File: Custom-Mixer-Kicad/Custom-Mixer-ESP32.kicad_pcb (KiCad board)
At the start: 2 copper layers, 176.3 x 110.6 mm, 25 parts, among them J1 OLED1, J2 OLED2, J3 OLED3, J4 OLED4, J5 OLED5, SW1 RotaryEncoder_Switch, SW2 RotaryEncoder_Switch, U1 ESP32-DevKitC, U2 2717

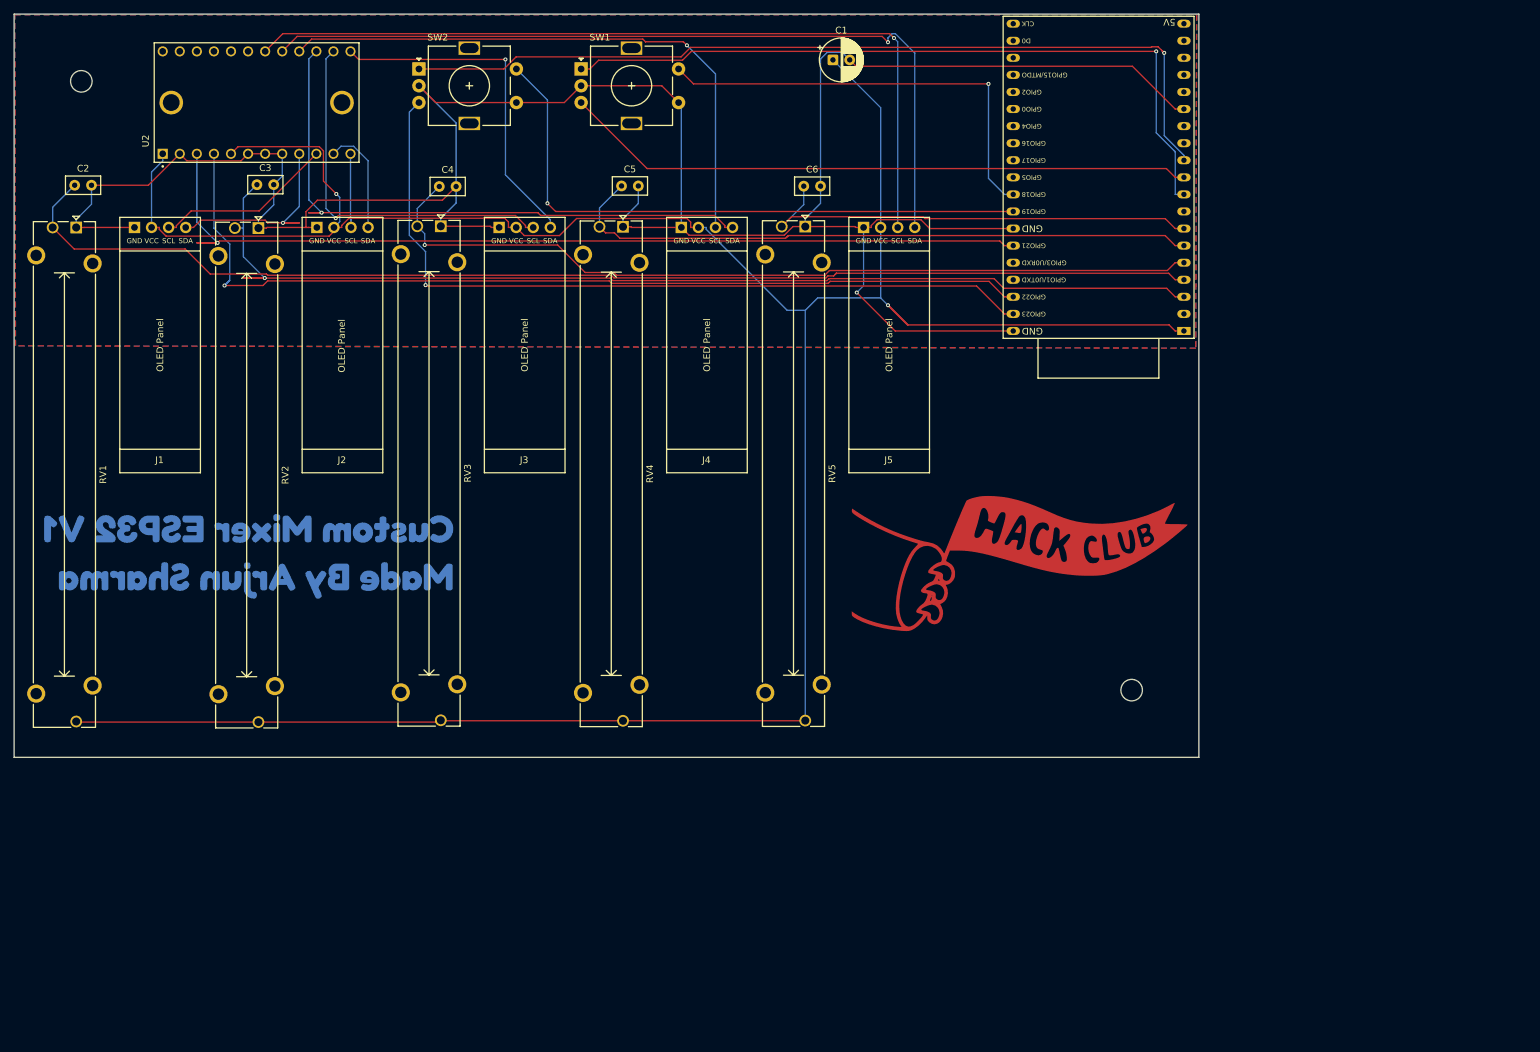
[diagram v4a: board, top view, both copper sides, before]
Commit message: Add MCP23017 PCB project & update KiCad libs
Add Adafruit MCP23017 GPIO Expander KiCad project (board, schematic, MCP23017 symbol/footprint, README, license, assets and pretty library parts). Add OLED 128x64 symbol/module files. Modify Custom-Mixer-ESP32 schematic and PCB, and update fp-lib-table and sym-lib-table to include the new parts and libraries.
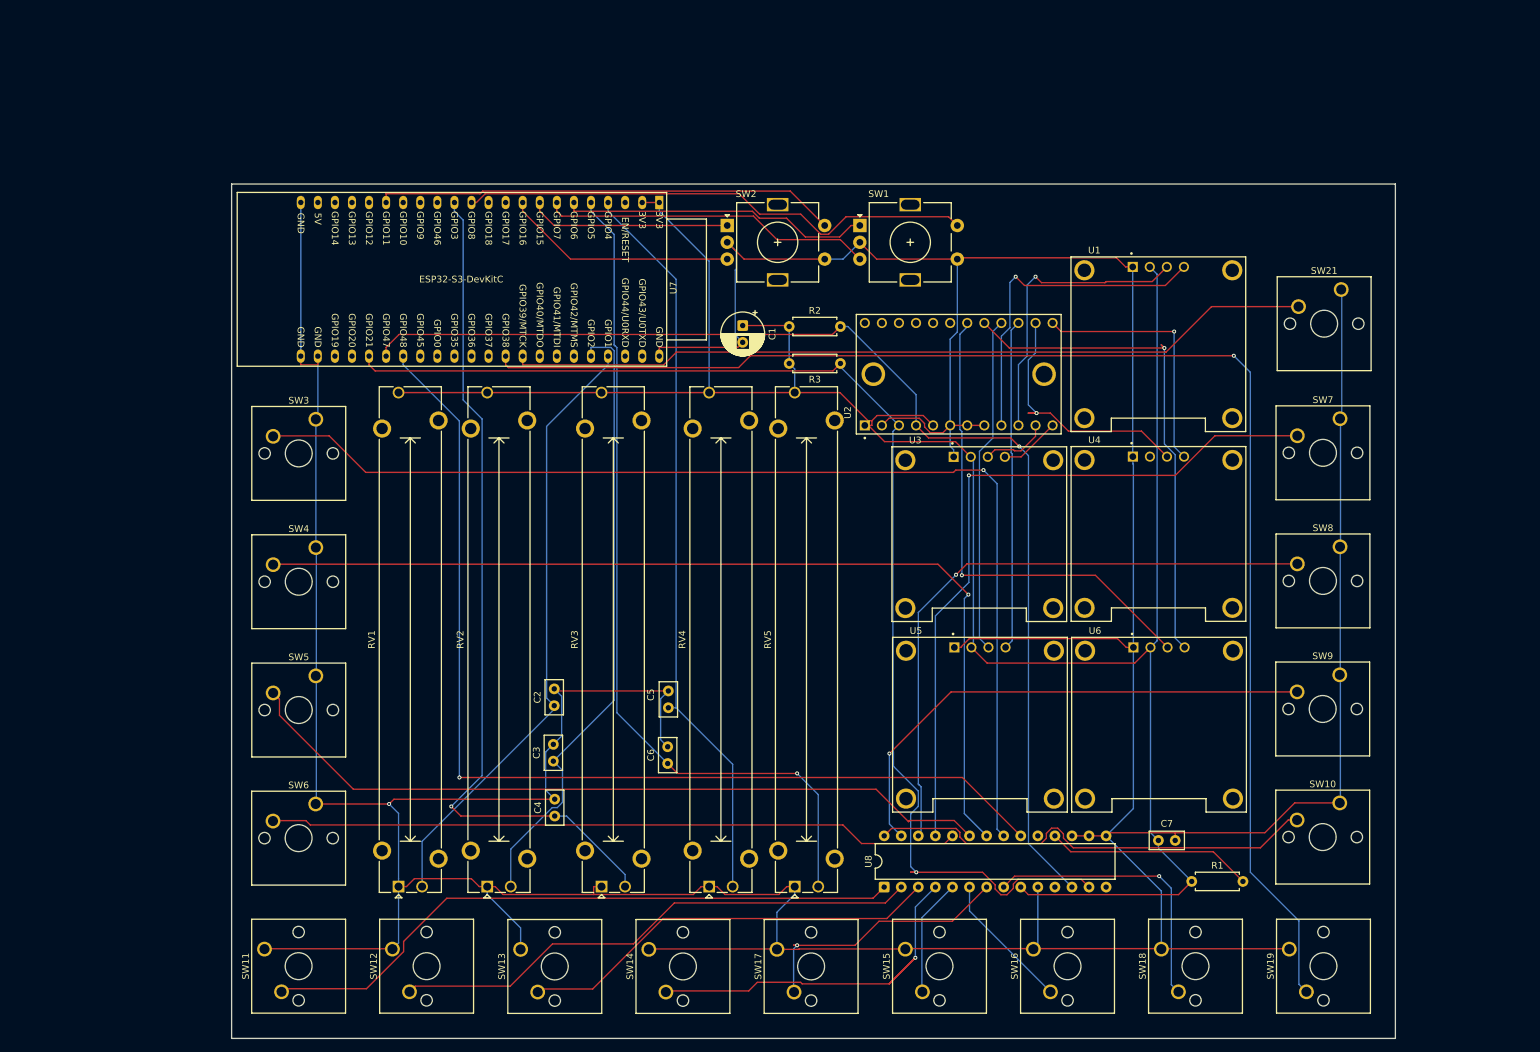
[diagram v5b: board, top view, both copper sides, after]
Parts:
- removed G***: LOGO, Custom-Mixer-Kicad:Hackclublogo(fmask)
- removed Hackclublogo: LOGO, Custom-Mixer-Kicad:Hackclublogo
- removed J1: OLED1, KiCad-SSD1306-0.91-OLED-4pin-128x32:SSD1306-0.91-OLED-4pin-128x32
- removed J2: OLED2, KiCad-SSD1306-0.91-OLED-4pin-128x32:SSD1306-0.91-OLED-4pin-128x32
- removed J3: OLED3, KiCad-SSD1306-0.91-OLED-4pin-128x32:SSD1306-0.91-OLED-4pin-128x32
- removed J4: OLED4, KiCad-SSD1306-0.91-OLED-4pin-128x32:SSD1306-0.91-OLED-4pin-128x32
- removed J5: OLED5, KiCad-SSD1306-0.91-OLED-4pin-128x32:SSD1306-0.91-OLED-4pin-128x32
- removed REF1, REF2: MountingHole_3.2mm_M3, MountingHole:MountingHole_3.2mm_M3
- removed kibuzzard-697B9E82: G***, kibuzzard-697B9E82
- added C7: 0.1µF, Capacitor_THT:C_Disc_D5.0mm_W2.5mm_P2.50mm, F.Cu at (235.6, 157.2)
- added R1: 10K, Resistor_THT:R_Axial_DIN0207_L6.3mm_D2.5mm_P7.62mm_Horizontal, F.Cu at (240.6, 163.3)
- added R2: 4.7K, Resistor_THT:R_Axial_DIN0207_L6.3mm_D2.5mm_P7.62mm_Horizontal, F.Cu at (180.7, 80.7)
- added R3: 4.7K, Resistor_THT:R_Axial_DIN0207_L6.3mm_D2.5mm_P7.62mm_Horizontal, F.Cu at (188.3, 86.2)
- added SW10: SW_Push, Button_Switch_Keyboard:SW_Cherry_MX_1.00u_PCB, F.Cu at (262.6, 151.6)
- added SW11: SW_Push, Button_Switch_Keyboard:SW_Cherry_MX_1.00u_PCB, F.Cu at (102.6, 173.3)
- added SW12: SW_Push, Button_Switch_Keyboard:SW_Cherry_MX_1.00u_PCB, F.Cu at (121.6, 173.3)
- added SW13: SW_Push, Button_Switch_Keyboard:SW_Cherry_MX_1.00u_PCB, F.Cu at (140.7, 173.4)
- added SW14: SW_Push, Button_Switch_Keyboard:SW_Cherry_MX_1.00u_PCB, F.Cu at (159.8, 173.4)
- added SW15: SW_Push, Button_Switch_Keyboard:SW_Cherry_MX_1.00u_PCB, F.Cu at (197.9, 173.3)
- added SW16: SW_Push, Button_Switch_Keyboard:SW_Cherry_MX_1.00u_PCB, F.Cu at (217.0, 173.3)
- added SW17: SW_Push, Button_Switch_Keyboard:SW_Cherry_MX_1.00u_PCB, F.Cu at (178.8, 173.4)
- added SW18: SW_Push, Button_Switch_Keyboard:SW_Cherry_MX_1.00u_PCB, F.Cu at (236.0, 173.3)
- added SW19: SW_Push, Button_Switch_Keyboard:SW_Cherry_MX_1.00u_PCB, F.Cu at (255.1, 173.3)
- added SW21: SW_Push, Button_Switch_Keyboard:SW_Cherry_MX_1.00u_PCB, F.Cu at (262.8, 75.2)
- added SW3: SW_Push, Button_Switch_Keyboard:SW_Cherry_MX_1.00u_PCB, F.Cu at (110.2, 94.5)
- added SW4: SW_Push, Button_Switch_Keyboard:SW_Cherry_MX_1.00u_PCB, F.Cu at (110.2, 113.6)
- added SW5: SW_Push, Button_Switch_Keyboard:SW_Cherry_MX_1.00u_PCB, F.Cu at (110.2, 132.7)
- added SW6: SW_Push, Button_Switch_Keyboard:SW_Cherry_MX_1.00u_PCB, F.Cu at (110.2, 151.7)
- added SW7: SW_Push, Button_Switch_Keyboard:SW_Cherry_MX_1.00u_PCB, F.Cu at (262.6, 94.4)
- added SW8: SW_Push, Button_Switch_Keyboard:SW_Cherry_MX_1.00u_PCB, F.Cu at (262.6, 113.5)
- added SW9: SW_Push, Button_Switch_Keyboard:SW_Cherry_MX_1.00u_PCB, F.Cu at (262.6, 132.5)
- added U3: DM-OLED096-636, Oled Screen 128x64:MODULE_DM-OLED096-636, F.Cu at (208.9, 111.6)
- added U4: DM-OLED096-636, Oled Screen 128x64:MODULE_DM-OLED096-636, F.Cu at (235.6, 111.6)
- added U5: DM-OLED096-636, Oled Screen 128x64:MODULE_DM-OLED096-636, F.Cu at (209.0, 139.9)
- added U6: DM-OLED096-636, Oled Screen 128x64:MODULE_DM-OLED096-636, F.Cu at (235.7, 139.9)
- added U7: ESP32-S3-DevKitC, PCM_Espressif:ESP32-S3-DevKitC, F.Cu at (161.3, 62.2)
- added U8: MCP23017_SP, Package_DIP:DIP-28_W7.62mm, F.Cu at (194.8, 164.1)
- U1: value ESP32-DevKitC -> DM-OLED096-636; footprint PCM_Espressif:ESP32-DevKitC -> Oled Screen 128x64:MODULE_DM-OLED096-636
- moved U2 112.0 mm to (205.9, 87.8)
- moved RV1 109.2 mm to (122.5, 164.0), turned to 90 degrees
- moved C2 105.3 mm to (145.7, 137.1), turned to 90 degrees
- moved RV2 103.7 mm to (135.7, 164.0), turned to 90 degrees
- moved RV3 101.1 mm to (152.7, 164.0), turned to 90 degrees
- moved RV4 99.0 mm to (168.8, 164.0), turned to 90 degrees
- moved RV5 98.2 mm to (181.5, 164.0), turned to 90 degrees
- moved C3 96.4 mm to (145.6, 145.4), turned to 90 degrees
- moved C4 95.2 mm to (145.8, 153.5), turned to 90 degrees
- moved C6 88.3 mm to (162.6, 145.7), turned to 90 degrees
- moved C5 77.9 mm to (162.7, 137.4), turned to 90 degrees
- moved SW2 51.4 mm to (171.4, 65.7)
- moved SW1 47.6 mm to (191.2, 65.7)
- moved C1 41.7 mm to (173.7, 80.6), turned to -90 degrees
- moved U1 4.29 mm to (235.6, 83.3), turned to 0 degrees
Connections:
- C2 pad 1: Net-(U1-SENSOR_VN/GPIO39/ADC1_CH3) -> GPIO 1
- C3 pad 1: Net-(U1-SENSOR_VP/GPIO36/ADC1_CH0) -> GPIO 2
- C4 pad 1: Net-(U1-VDET_1/GPIO34/ADC1_CH6) -> GPIO 3
- C5 pad 1: Net-(U1-VDET_2/GPIO35/ADC1_CH7) -> GPIO 4
- C6 pad 1: Net-(U1-32K_XP/GPIO32/ADC1_CH4) -> GPIO 5
- RV1 pad 2: Net-(U1-SENSOR_VN/GPIO39/ADC1_CH3) -> GPIO 1
- RV2 pad 2: Net-(U1-SENSOR_VP/GPIO36/ADC1_CH0) -> GPIO 2
- RV3 pad 2: Net-(U1-VDET_1/GPIO34/ADC1_CH6) -> GPIO 3
- RV4 pad 2: Net-(U1-VDET_2/GPIO35/ADC1_CH7) -> GPIO 4
- RV5 pad 2: Net-(U1-32K_XP/GPIO32/ADC1_CH4) -> GPIO 5
- SW1 pad A: Net-(U1-DAC_1/ADC2_CH8/GPIO25) -> GPIO 6
- SW1 pad B: Net-(U1-DAC_2/ADC2_CH9/GPIO26) -> GPIO 7
- SW1 pad S2: Net-(U1-GPIO18) -> GPIO 8
- SW2 pad A: Net-(U1-ADC2_CH7/GPIO27) -> GPIO 15
- SW2 pad B: Net-(U1-GPIO23) -> GPIO 16
- SW2 pad S2: Net-(U1-GPIO19) -> GPIO 17
- U1 pad 1: +3V3 -> GND
- U1 pad 2: unconnected-(U1-CHIP_PU-Pad2) -> +3V3
- U1 pad 3: Net-(U1-SENSOR_VP/GPIO36/ADC1_CH0) -> Net-(U1-SCL)
- U1 pad 4: Net-(U1-SENSOR_VN/GPIO39/ADC1_CH3) -> Net-(U1-SDA)
- U2 pad 10: Net-(J1-Pin_3) -> Net-(U1-SCL)
- U2 pad 3: Net-(U1-GPIO21) -> SDA
- U2 pad 4: Net-(U1-GPIO22) -> SCL
- U2 pad 9: Net-(J1-Pin_4) -> Net-(U1-SDA)
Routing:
- net GND: track 374.9 -> 805.6 mm
- net GPIO 38: track 0.00 -> 209.6 mm, vias 0 -> 1
- net SDA: track 0.00 -> 186.9 mm, vias 0 -> 1
- net Net-(U1-SENSOR_VN/GPIO39/ADC1_CH3): track 180.0 -> 0.00 mm
- net SCL: track 0.00 -> 175.7 mm, vias 0 -> 1
- net Net-(U1-SENSOR_VP/GPIO36/ADC1_CH0): track 168.3 -> 0.00 mm, vias 1 -> 0
- net a0: track 0.00 -> 163.8 mm, vias 0 -> 1
- net Net-(U7-GPIO48): track 0.00 -> 153.3 mm, vias 0 -> 1
- net Net-(U1-GPIO21): track 145.6 -> 0.00 mm, vias 1 -> 0
- net a1: track 0.00 -> 142.9 mm, vias 0 -> 1
- net Net-(U1-GPIO22): track 141.8 -> 0.00 mm, vias 1 -> 0
- net Net-(U1-ADC2_CH7/GPIO27): track 131.9 -> 0.00 mm, vias 1 -> 0
- net GPIO 5: track 0.00 -> 126.4 mm, vias 0 -> 1
- net Net-(U1-VDET_1/GPIO34/ADC1_CH6): track 126.1 -> 0.00 mm, vias 1 -> 0
- net GPIO 3: track 0.00 -> 125.3 mm, vias 0 -> 1
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- removed copper zone on B.Cu, net GND
- removed copper zone on F.Cu, net GND
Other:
- board size 176.3 x 110.6 mm -> 173.2 x 127.1 mm

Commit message: Rewire and create custom footprint
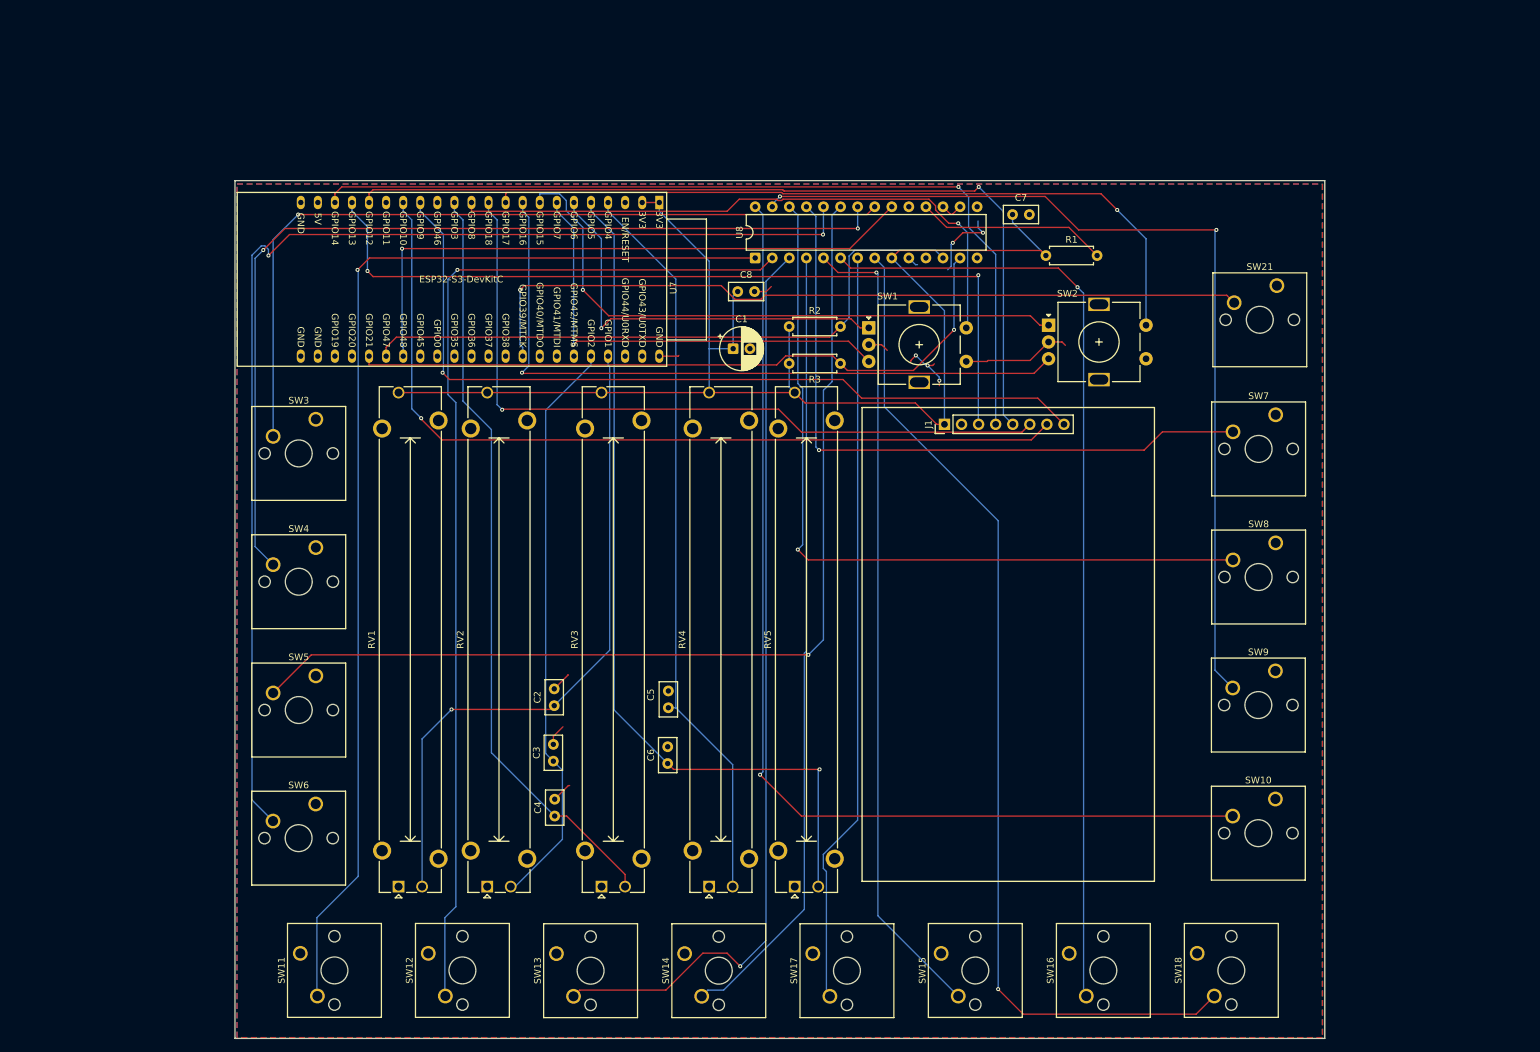
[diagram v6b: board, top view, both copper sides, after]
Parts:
- removed SW19: SW_Push, Button_Switch_Keyboard:SW_Cherry_MX_1.00u_PCB
- removed U1, U3, U4, U5, U6: DM-OLED096-636, Oled Screen 128x64:MODULE_DM-OLED096-636
- removed U2: 2717, TCA9548A Breakout:MODULE_2717
- added C8: 0.1µF, Capacitor_THT:C_Disc_D5.0mm_W2.5mm_P2.50mm, F.Cu at (173.0, 75.5)
- added J1: Conn_01x08, Connector_PinHeader_2.54mm:PinHeader_1x08_P2.54mm_Vertical, F.Cu at (203.8, 95.2)
- moved C7 95.6 mm to (213.9, 64.0)
- moved R1 95.6 mm to (218.8, 70.1)
- moved U8 95.5 mm to (175.6, 70.5)
- moved SW2 50.1 mm to (219.2, 80.5)
- moved SW1 15.3 mm to (192.5, 80.9)
- moved SW10 9.59 mm to (253.0, 151.0)
- moved SW21 9.59 mm to (253.2, 74.6)
- moved SW9 9.59 mm to (253.0, 131.9)
- moved SW7 9.59 mm to (253.0, 93.8)
- moved SW8 9.59 mm to (253.0, 112.9)
- moved SW13 5.37 mm to (146.0, 174.0)
- moved SW15 5.37 mm to (203.3, 174.0)
- moved SW18 5.37 mm to (241.4, 174.0)
- moved SW11 5.37 mm to (107.9, 174.0)
- moved SW12 5.37 mm to (127.0, 174.0)
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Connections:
- U7 pad 10: unconnected-(U7-GPIO17/ADC2_CH6-Pad10) -> GPIO 17
- U7 pad 11: unconnected-(U7-GPIO18/ADC2_CH7-Pad11) -> DC
- U7 pad 15: unconnected-(U7-GPIO9/ADC1_CH8-Pad15) -> BL
- U7 pad 16: unconnected-(U7-GPIO10/ADC1_CH9-Pad16) -> RST
- U7 pad 17: GPIO 17 -> GPIO 11
- U7 pad 18: unconnected-(U7-GPIO12/ADC2_CH1-Pad18) -> CS
- U7 pad 19: unconnected-(U7-GPIO13/ADC2_CH2-Pad19) -> MOSI
- U7 pad 20: unconnected-(U7-GPIO14/ADC2_CH3-Pad20) -> CLK
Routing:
- net GND: track 805.6 -> 59.4 mm, vias 1 -> 5
- net GPIO 38: track 209.6 -> 0.00 mm, vias 1 -> 0
- net +3V3: track 331.9 -> 199.4 mm
- net CLK: track 0.00 -> 132.1 mm, vias 0 -> 1
- net CS: track 0.00 -> 130.0 mm, vias 0 -> 1
- net RST: track 0.00 -> 128.7 mm, vias 0 -> 1
- net MOSI: track 0.00 -> 124.7 mm, vias 0 -> 2
- net b5: track 20.6 -> 143.1 mm, vias 0 -> 1
- net BL: track 0.00 -> 122.4 mm, vias 0 -> 1
- net DC: track 0.00 -> 112.1 mm, vias 0 -> 1
- net b7: track 42.2 -> 151.2 mm
- net b4: track 17.5 -> 121.5 mm, vias 0 -> 1
- net a7: track 67.9 -> 158.0 mm, vias 0 -> 1
- net SDA: track 186.9 -> 103.4 mm
- net SCL: track 175.7 -> 96.0 mm, vias 1 -> 0
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- added copper zone on B.Cu, net GND
- added copper zone on F.Cu, net GND
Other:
- board size 173.2 x 127.1 mm -> 162.2 x 127.6 mm

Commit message: Update Custom-Mixer-ESP32.kicad_pcb
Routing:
- net GND: track 59.4 -> 675.1 mm, vias 5 -> 0
- net Net-(U7-GPIO48): track 91.5 -> 106.8 mm
- net a4: track 99.7 -> 112.6 mm
- net GPIO 3: track 113.3 -> 124.3 mm, vias 0 -> 1
- net a2: track 150.6 -> 159.3 mm
- net a6: track 138.3 -> 130.9 mm, vias 2 -> 1
- net BL: track 122.4 -> 129.6 mm
- net a0: track 120.8 -> 127.5 mm
- net GPIO 16: track 105.4 -> 98.7 mm
- net GPIO 5: track 128.7 -> 122.8 mm
- net a3: track 177.6 -> 183.0 mm, vias 2 -> 1
- net a1: track 141.5 -> 146.4 mm, vias 2 -> 1
- net RST: track 128.7 -> 123.8 mm
- net a5: track 117.5 -> 122.3 mm, vias 1 -> 2
- net MOSI: track 124.7 -> 120.4 mm, vias 2 -> 1
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- removed copper zone on B.Cu, net GND
- removed copper zone on F.Cu, net GND

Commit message: Complete Wire Revamp
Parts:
- added SW19: SW_Push, Button_Switch_Keyboard:SW_Cherry_MX_1.00u_PCB, F.Cu at (281.4, 160.8)
- added kibuzzard-6987AAB7: G***, kibuzzard-6987AAB7, B.Cu at (201.1, 107.1)
- moved SW11 169.7 mm to (262.4, 103.6), turned to 0 degrees
- moved SW17 145.7 mm to (281.4, 65.5), turned to 0 degrees
- moved SW12 144.8 mm to (262.4, 122.7), turned to 0 degrees
- moved SW3 136.3 mm to (243.4, 65.5)
- moved SW4 136.3 mm to (243.4, 84.6)
- moved SW5 136.3 mm to (243.4, 103.7)
- moved SW6 136.3 mm to (243.4, 122.7)
- moved SW13 120.7 mm to (262.4, 141.8), turned to 0 degrees
- moved SW15 118.8 mm to (281.5, 84.6), turned to 0 degrees
- moved C7 103.9 mm to (207.3, 167.7)
- moved SW14 98.2 mm to (262.4, 160.8), turned to 0 degrees
- moved U8 94.2 mm to (186.7, 164.1)
- moved R1 94.2 mm to (225.0, 164.1), turned to 90 degrees
- moved SW16 91.9 mm to (281.5, 103.7), turned to 0 degrees
- moved SW21 72.8 mm to (281.5, 141.8)
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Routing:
- net GND: track 675.1 -> 157.9 mm, vias 0 -> 5
- net GPIO 40: track 0.00 -> 264.4 mm, vias 0 -> 1
- net a3: track 183.0 -> 69.2 mm
- net SCL: track 93.9 -> 200.6 mm, vias 1 -> 3
- net SDA: track 107.1 -> 211.3 mm, vias 1 -> 3
- net GPIO 7: track 71.0 -> 149.7 mm
- net GPIO 6: track 61.3 -> 138.1 mm
- net GPIO 8: track 90.2 -> 166.7 mm
- net a5: track 122.3 -> 48.1 mm, vias 2 -> 0
- net a2: track 159.3 -> 88.7 mm
- net GPIO 39: track 114.9 -> 182.2 mm
- net a4: track 112.6 -> 51.1 mm
- net +3V3: track 202.8 -> 262.5 mm, vias 0 -> 1
- net b6: track 112.0 -> 167.9 mm, vias 0 -> 2
- net b1: track 159.1 -> 103.6 mm
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- added copper zone on B.Cu, net GND
- added copper zone on F.Cu, net GND
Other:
- board size 162.2 x 127.6 mm -> 192.1 x 118.4 mm
